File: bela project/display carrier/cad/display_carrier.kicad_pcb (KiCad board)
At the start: 2 copper layers, 186.1 x 72.8 mm, 6 parts, among them U1 PocketBeagle2

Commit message: display carrier: hex standoffs + mounting holes; book gets Chapter 02 (dual-screen board)
Grew the carrier to 194x81mm with a 7mm mounting border + 4x M2.5 corner holes
(add_mounts.py, on the routed board - routing untouched, holes in the bare margin so
no re-pour). Modelled 4 brass M2.5 hex standoffs carrying the wide board level above
the sandwich, rendered into the assembled stack. Added Chapter 02 "The dual-screen
carrier" to the build-journal book: the two T-Display-S3 Long AMOLED bars, six design
decisions, the male-header connection, the ~36mm stack-height note, and a full BOM at
the end of the section. Refreshed ensemble renders (now with the standoffs).

Co-Authored-By: Claude Opus 4.8 (1M context) <noreply@anthropic.com>
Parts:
- added H1: MountingHole_2.7mm_M2.5, MountingHole_2.7mm_M2.5, F.Cu at (3.70, 6.10)
- added H2: MountingHole_2.7mm_M2.5, MountingHole_2.7mm_M2.5, F.Cu at (192.8, 6.10)
- added H3: MountingHole_2.7mm_M2.5, MountingHole_2.7mm_M2.5, F.Cu at (3.70, 81.9)
- added H4: MountingHole_2.7mm_M2.5, MountingHole_2.7mm_M2.5, F.Cu at (192.8, 81.9)
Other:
- board size 186.1 x 72.8 mm -> 194.1 x 80.8 mm

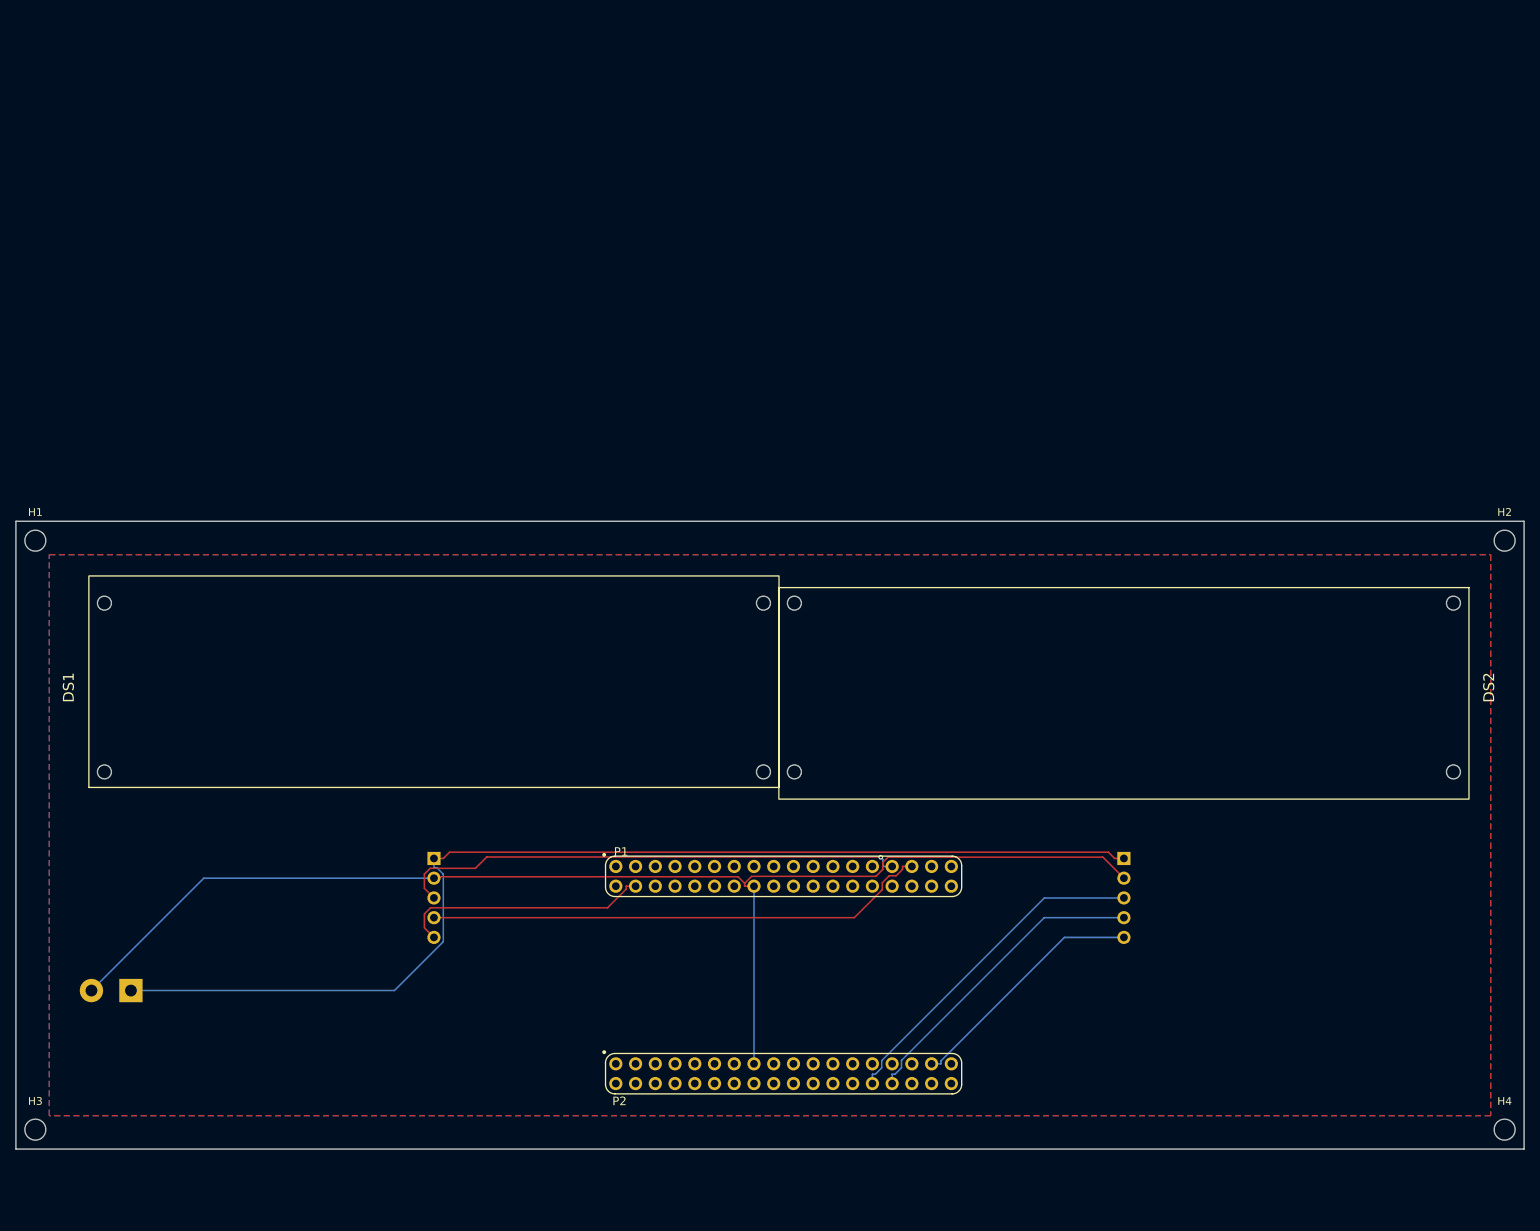
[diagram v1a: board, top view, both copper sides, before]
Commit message: carrier: MIDI ribbon HUB (J_MIDI) + full-ensemble STEP with all jacks for MoI3D
Added J_MIDI (2x3 IDC) to the display carrier so the MIDI board's ribbon plugs into the
carrier UNDERSIDE and is distributed down via U1 to free Beagle pins (+3V3=P2.23,
RX=P2.32, TX=P2.34 - UART4 is taken by the Bela's audio, so MIDI is soft-serial like
the displays). Re-routed (0.25mm, 83 tracks, 0 unconnected, board 194x89mm). Rebuilt
XOVND_ensemble.step (~630 solids): all 4 boards positioned + 4 hex standoffs + ribbon,
with the MIDI board flipped 180deg so its TRS jacks face the front panel. The Lumberg
1503 jack 3D model isn't installed in this KiCad, so neither the MIDI nor the Bela audio
jacks render - added box+barrel approximations (bl_addjacks.py + the STEP merge) so all
four minijacks are visible. Refreshed ensemble + jack renders.

Co-Authored-By: Claude Opus 4.8 (1M context) <noreply@anthropic.com>
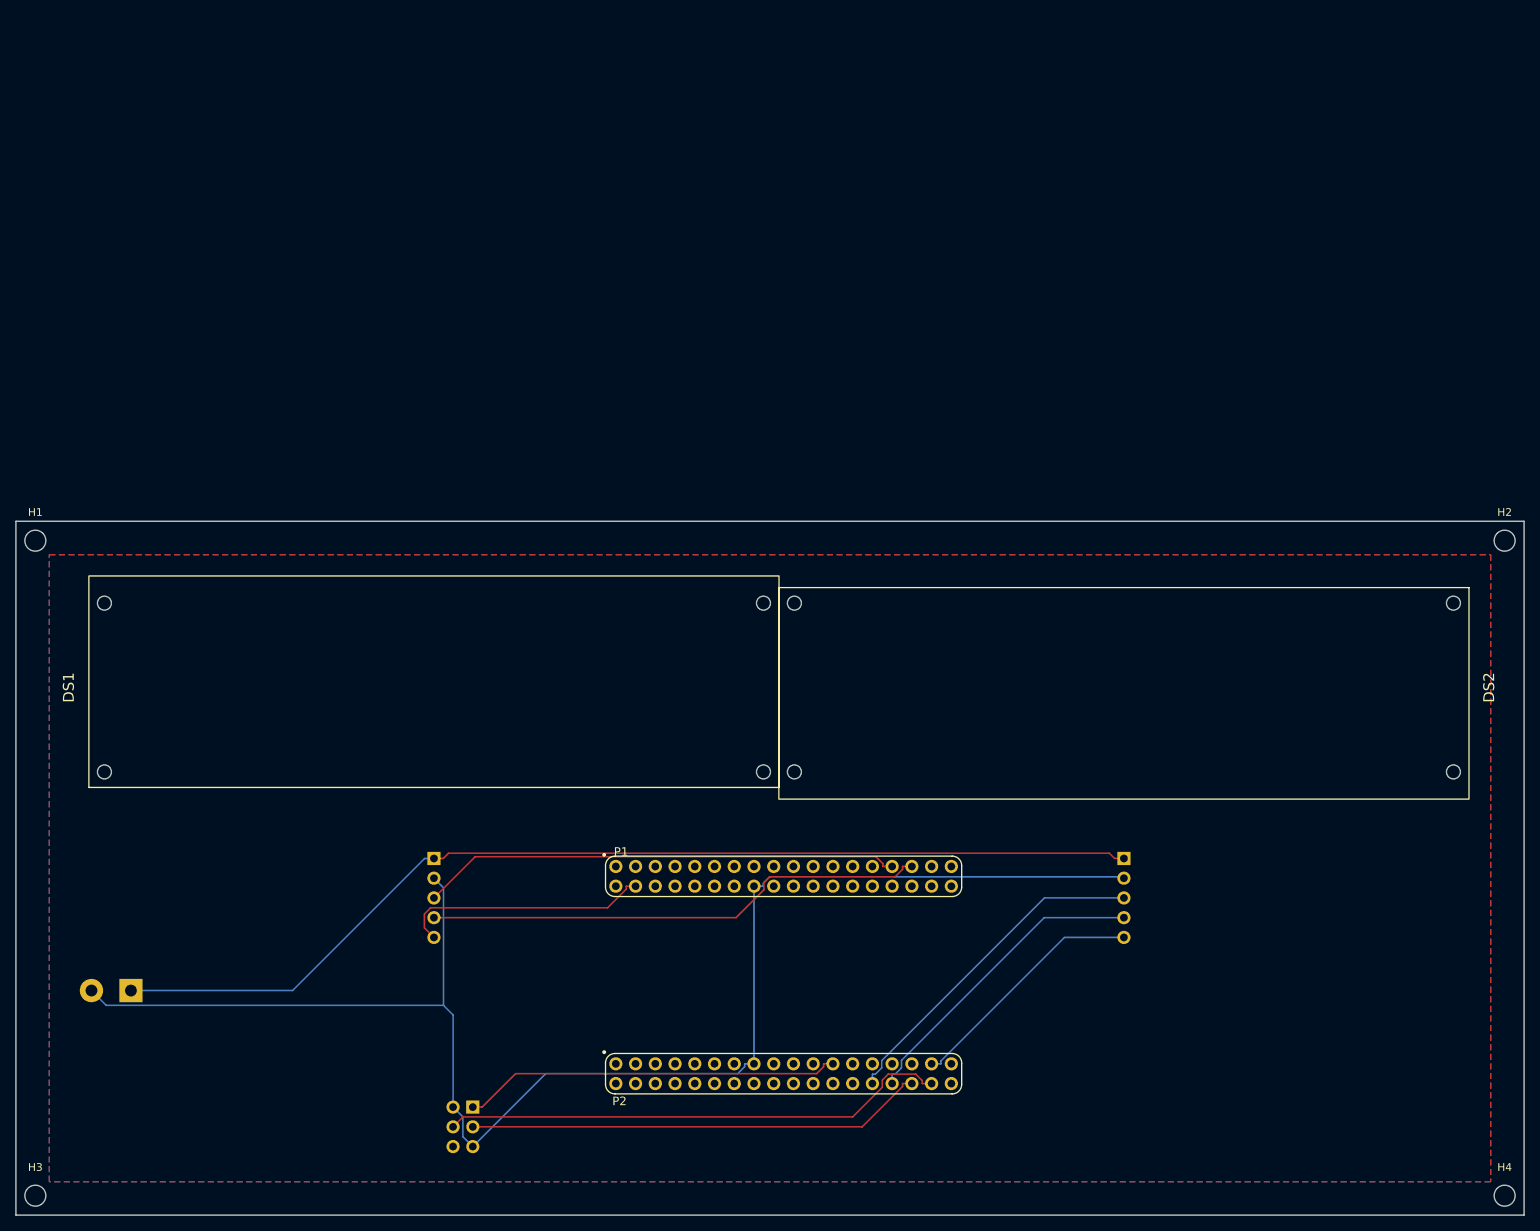
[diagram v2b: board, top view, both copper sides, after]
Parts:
- added J_MIDI: MIDI_HUB, PinHeader_2x03_P2.54mm_Vertical, B.Cu at (60.0, 79.0)
- moved H3 8.50 mm to (3.70, 90.4)
- moved H4 8.50 mm to (192.8, 90.4)
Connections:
- U1 pad P2.23: (no net) -> +3V3
- U1 pad P2.32: (no net) -> MIDI_RX
- U1 pad P2.34: (no net) -> MIDI_TX
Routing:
- net MIDI_TX: track 0.00 -> 65.7 mm
- net MIDI_RX: track 0.00 -> 59.0 mm
- net +3V3: track 0.00 -> 48.9 mm
- net GND: track 166.8 -> 194.8 mm
- net +5V: track 143.7 -> 135.4 mm
- net DA_TX: track 65.7 -> 61.9 mm, vias 1 -> 0
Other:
- board size 194.1 x 80.8 mm -> 194.1 x 89.3 mm

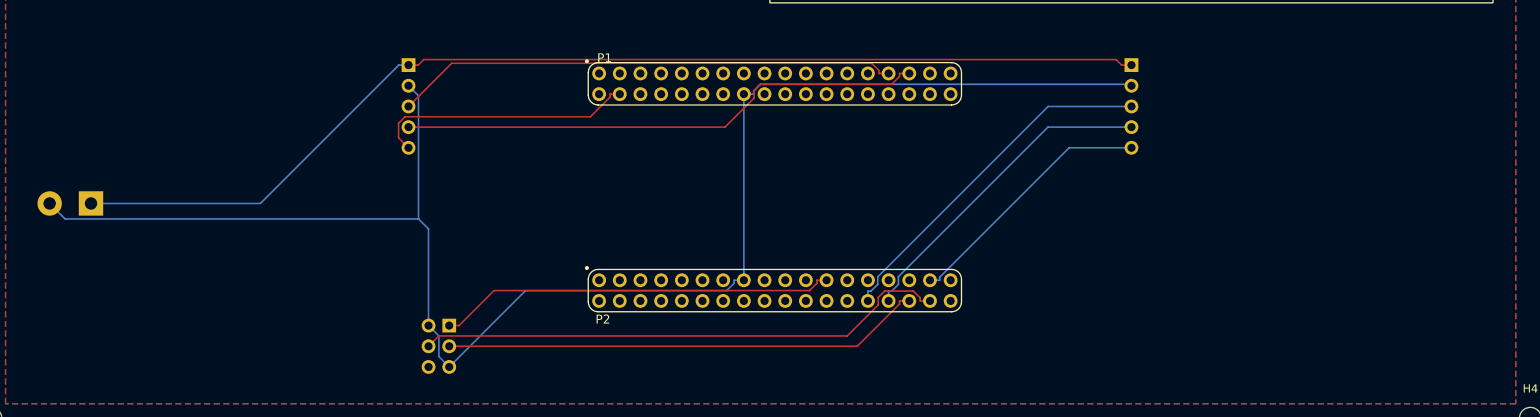
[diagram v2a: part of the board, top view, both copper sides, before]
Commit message: carrier: fly the sandwich to the right edge so the Bela audio jacks are accessible
The wide carrier buried the Bela's audio jacks ~68mm inside. Moved U1 on the carrier to
the right edge (KiCad x 100->165, below DS2; JB 143.8->110 to clear it) so the Beagle+Bela
sandwich sits at that edge and the audio jacks reach a free panel edge (barrel to world
x~59, carrier edge ~58). Re-routed clean (0 unconnected, 87 tracks). Trade-off, accepted:
the two displays are now asymmetric (left of the sandwich). Ensemble transforms updated
(G_CARRIER -137, MIDI relocated front-left by the moved J_MIDI), STEP re-merged, renders
refreshed. Also fixed the Lumberg jack model (not shipped with this KiCad) - gen_jack.py
generates it and the MIDI footprint points at it, so J1/J2 render natively too.

Co-Authored-By: Claude Opus 4.8 (1M context) <noreply@anthropic.com>
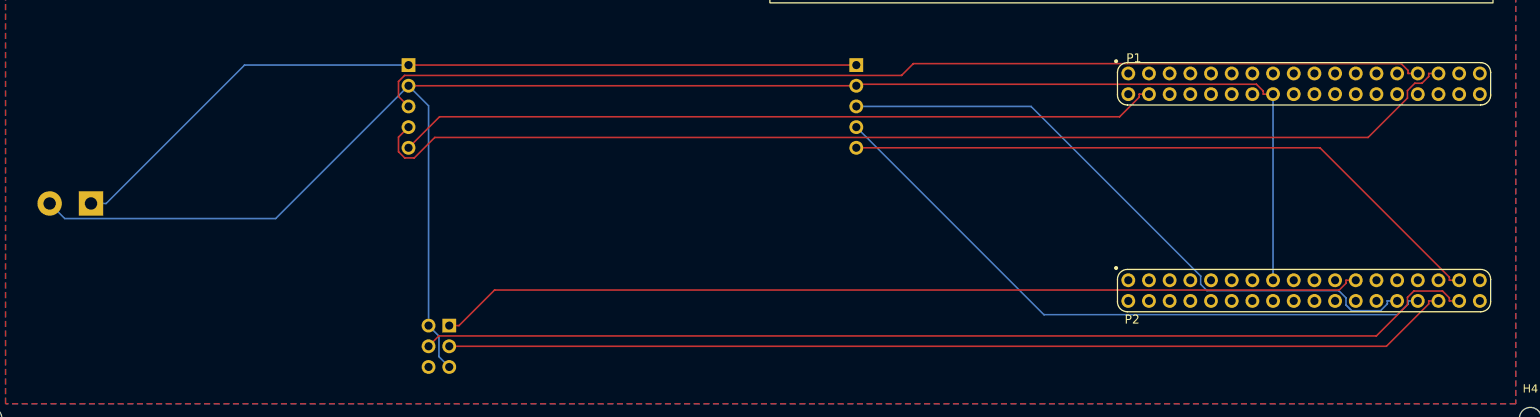
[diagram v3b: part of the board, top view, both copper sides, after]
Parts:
- moved U1 65.0 mm to (165.0, 62.0)
- moved JB 33.8 mm to (110.0, 47.0)
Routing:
- net DA_RX: track 65.0 -> 136.6 mm
- net DA_TX: track 61.9 -> 130.4 mm
- net +3V3: track 48.9 -> 113.9 mm
- net MIDI_RX: track 59.0 -> 124.0 mm
- net MIDI_TX: track 65.7 -> 130.7 mm
- net DA_RST: track 32.4 -> 93.9 mm
- net DB_RST: track 31.7 -> 81.0 mm
- net DB_RX: track 39.9 -> 79.4 mm
- net DB_TX: track 43.5 -> 78.6 mm
- net +5V: track 135.4 -> 101.0 mm
- net GND: track 194.8 -> 218.1 mm

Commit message: carrier: JA/JB become FEMALE sockets on the front so the displays plug in for power+data
The displays had no direct connector - JA/JB were male cable headers on the back. Changed
them to FEMALE PinSocket_1x05 on F.Cu (the display side), in the gap just below each panel,
so each T-Display module plugs straight in for +5V/GND/TX/RX/RST (no cable). JB is offset
left (x110->120) to clear the edge-shifted U1 - fixed a pad/hole/mask collision + 2
unconnected that came from JB overlapping U1's pins. Re-routed clean (0 unconnected, 80
tracks, 0 hard DRC). GLB/STEP + ensemble re-exported; socket position should be matched to
the LILYGO module's real breakout header.

Co-Authored-By: Claude Opus 4.8 (1M context) <noreply@anthropic.com>
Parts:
- removed the JA at (55.0, 47.0)
- removed the JB at (110.0, 47.0)
- added JA: DISP_A, PinSocket_1x05_P2.54mm_Vertical, F.Cu at (55.0, 43.0)
- added JB: DISP_B, PinSocket_1x05_P2.54mm_Vertical, F.Cu at (120.0, 43.0)
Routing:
- net +5V: track 101.0 -> 112.7 mm
- net DB_RX: track 79.4 -> 70.2 mm
- net DA_RX: track 136.6 -> 127.8 mm
- net DB_RST: track 81.0 -> 72.7 mm
- net DA_TX: track 130.4 -> 125.2 mm
- net DB_TX: track 78.6 -> 73.9 mm
- net DA_RST: track 93.9 -> 92.2 mm
- net MIDI_TX: track 130.7 -> 130.1 mm
- net +3V3: track 113.9 -> 114.4 mm

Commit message: display carrier: align JA/JB sockets to the LILYGO P5 connector (coincident + exact)
The P5 panel sockets were placed from an assumed module-frame P5 centre, which
put them ~12.6 mm off the display's actual factory connector. Measured the real
H685 P5 body positions in the exported STEP (DS1 (69.9,31.3), DS2 (128.9,18.7))
and moved JA/JB so each socket's pad-centre sits coincident with the module's P5,
to ±0.1 mm — the male P5 now inserts into the socket receptacle and each panel
seats at its true sandwiched height. JA/JB are now 2x15 P1.27 mm PinSockets that
mirror the LILYGO P5 pin-for-pin (was a mis-scoped 1x5). Re-routed clean (0
unconnected, 0 hard DRC), re-exported GLB + STEP, re-merged XOVND_ensemble.step,
rebuilt the Blender stack. Refreshed the build-journal book (JA/JB text + BOM +
carrier renders). Removed the dead 1x5 footprints.

Co-Authored-By: Claude Opus 4.8 (1M context) <noreply@anthropic.com>
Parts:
- removed the JA at (55.0, 43.0)
- removed the JB at (120.0, 43.0)
- added JA: DISP_A, PinSocket_2x15_P1.27mm_Vertical, F.Cu at (61.0, 30.7)
- added JB: DISP_B, PinSocket_2x15_P1.27mm_Vertical, F.Cu at (137.8, 19.3)
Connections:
- U1 pad P1.4: DA_RST -> (no net)
- U1 pad P2.33: DB_RST -> (no net)
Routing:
- net DA_RST: track 92.2 -> 0.00 mm
- net DB_RST: track 72.7 -> 0.00 mm
- net GND: track 218.1 -> 251.3 mm
- net DB_TX: track 73.9 -> 104.7 mm
- net DB_RX: track 70.2 -> 85.5 mm
- net +5V: track 112.7 -> 124.5 mm
- net DA_TX: track 125.2 -> 115.2 mm, vias 0 -> 1
- net DA_RX: track 127.8 -> 118.5 mm
- net MIDI_TX: track 130.1 -> 130.7 mm
- net +3V3: track 114.4 -> 113.9 mm
